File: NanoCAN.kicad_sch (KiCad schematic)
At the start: 18 parts, among them J2 Screw_Terminal_01x02, J3 Screw_Terminal_01x02, SW1 SW_DIP_x01, U1 MCP2557FD-xSN, U3 MCP2517FD-xJHA, Y1 Crystal_GND24

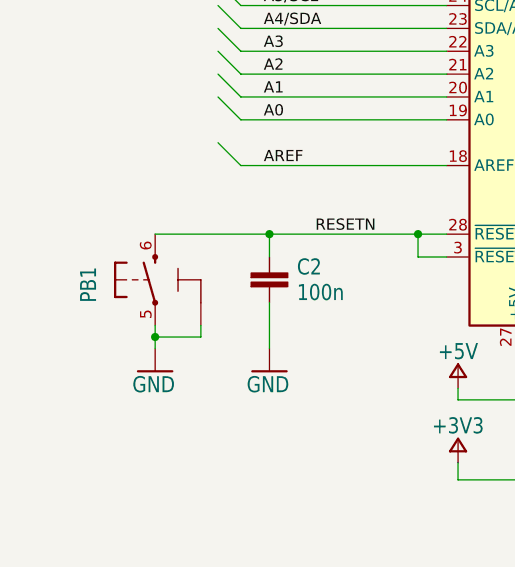
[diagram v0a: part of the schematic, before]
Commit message: Swap pushbutton for PTS810 and create 3D Model
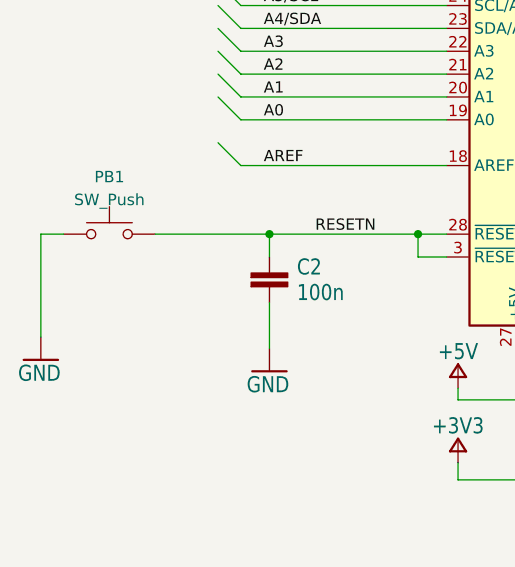
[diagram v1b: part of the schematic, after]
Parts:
- removed PB1: TACTILE1PTS820-NH, NANOEveryV3.0:C&K_PTS820_NO_HOLES, symbol NANOEveryV3.0-eagle-import:TACTILE1PTS820-NH
- added PB1: SW_Push, Button_Switch_SMD:SW_SPST_PTS810, symbol Switch:SW_Push
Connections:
- net GND: now also PB1.1
- net RESETN: now also PB1.2
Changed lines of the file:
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@@
   (junction (at 349.885 150.495) (diameter 0) (color 0 0 0 0)
   )
-  (junction (at 167.64 195.58) (diameter 0) (color 0 0 0 0)
-  )
   (junction (at 259.08 172.72) (diameter 0) (color 0 0 0 0)
   )
@@
     (stroke (width 0) (type default))
   )
-  (wire (pts (xy 172.72 195.58) (xy 172.72 194.31))
+  (wire (pts (xy 154.94 184.15) (xy 154.94 195.58))
     (stroke (width 0.1524) (type solid))
   )
@@
     (stroke (width 0) (type default))
   )
-  (wire (pts (xy 167.64 195.58) (xy 172.72 195.58))
-    (stroke (width 0.1524) (type solid))
-  )
   (wire (pts (xy 200.025 176.53) (xy 177.165 176.53))
     (stroke (width 0.1524) (type solid))
@@
     (stroke (width 0.1524) (type solid))
   )
-  (wire (pts (xy 167.64 194.31) (xy 167.64 195.58))
-    (stroke (width 0.1524) (type solid))
-  )
   (wire (pts (xy 309.88 161.29) (xy 333.375 161.29))
     (stroke (width 0) (type default))
@@
     (stroke (width 0) (type default))
   )
-  (wire (pts (xy 167.64 195.58) (xy 167.64 196.85))
-    (stroke (width 0.1524) (type solid))
-  )
   (wire (pts (xy 375.92 184.785) (xy 375.92 183.515))
     (stroke (width 0) (type default))
@@
   )
   (wire (pts (xy 225.425 173.99) (xy 245.745 173.99))
+    (stroke (width 0.1524) (type solid))
+  )
+  (wire (pts (xy 154.94 184.15) (xy 157.48 184.15))
     (stroke (width 0.1524) (type solid))
   )
@@
         (path "/a24b9486-fc79-44d2-a048-c84f452a13e3"
           (reference "#GND04") (unit 1)
+        )
+      )
+    )
+  )
+  (symbol (lib_id "Switch:SW_Push") (at 162.56 184.15 0) (unit 1)
+    (in_bom yes) (on_board yes) (dnp no) (fields_autoplaced)
+    (property "Reference" "PB1" (at 162.56 177.8 0)
+      (effects (font (size 1.27 1.27)))
+    )
+    (property "Value" "SW_Push" (at 162.56 180.34 0)
+      (effects (font (size 1.27 1.27)))
+    )
+    (property "Footprint" "Button_Switch_SMD:SW_SPST_PTS810" (at 162.56 179.07 0)
+      (effects (font (size 1.27 1.27)) hide)
+    )
+    (property "Datasheet" "~" (at 162.56 179.07 0)
+      (effects (font (size 1.27 1.27)) hide)
+    )
+    (pin "1")
+    (pin "2")
+    (instances
+      (project "NanoCAN"
+        (path "/a24b9486-fc79-44d2-a048-c84f452a13e3"
+          (reference "PB1") (unit 1)
         )
       )
@@
     )
   )
-  (symbol (lib_id "NANOEveryV3.0-eagle-import:TACTILE1PTS820-NH") (at 167.64 189.23 0) (unit 1)
-    (in_bom yes) (on_board yes) (dnp no)
-    (property "Reference" "PB1" (at 161.29 191.77 90)
-      (effects (font (size 1.778 1.5113)) (justify left bottom))
-    )
-    (property "Value" "TACTILE1PTS820-NH" (at 167.64 189.23 0)
-      (effects (font (size 1.27 1.27)) hide)
-    )
-    (property "Footprint" "NANOEveryV3.0:C&K_PTS820_NO_HOLES" (at 167.64 189.23 0)
-      (effects (font (size 1.27 1.27)) hide)
-    )
-    (property "Datasheet" "" (at 167.64 189.23 0)
-      (effects (font (size 1.27 1.27)) hide)
-    )
-    (pin "1")
-    (pin "2")
-    (pin "3")
-    (pin "4")
-    (pin "5")
-    (pin "6")
-    (instances
-      (project "NanoCAN"
-        (path "/a24b9486-fc79-44d2-a048-c84f452a13e3"
-          (reference "PB1") (unit 1)
-        )
-      )
-    )
-  )
   (symbol (lib_id "Device:R") (at 375.92 179.705 180) (unit 1)
     (in_bom yes) (on_board yes) (dnp no)
@@
     )
   )
-  (symbol (lib_id "NANOEveryV3.0-eagle-import:Arduino-supply_GND") (at 167.64 199.39 0) (unit 1)
-    (in_bom yes) (on_board yes) (dnp no)
-    (property "Reference" "#GND017" (at 167.64 199.39 0)
-      (effects (font (size 1.27 1.27)) hide)
-    )
-    (property "Value" "GND" (at 165.1 201.93 0)
+  (symbol (lib_id "NANOEveryV3.0-eagle-import:Arduino-supply_GND") (at 154.94 198.12 0) (unit 1)
+    (in_bom yes) (on_board yes) (dnp no)
+    (property "Reference" "#GND017" (at 154.94 198.12 0)
+      (effects (font (size 1.27 1.27)) hide)
+    )
+    (property "Value" "GND" (at 152.4 200.66 0)
       (effects (font (size 1.778 1.5113)) (justify left bottom))
     )
-    (property "Footprint" "" (at 167.64 199.39 0)
-      (effects (font (size 1.27 1.27)) hide)
-    )
-    (property "Datasheet" "" (at 167.64 199.39 0)
-      (effects (font (size 1.27 1.27)) hide)
-    )
+    (property "Footprint" "" (at 154.94 198.12 0)
+      (effects (font (size 1.27 1.27)) hide)
+    )
+    (property "Datasheet" "" (at 154.94 198.12 0)
+      (effects (font (size 1.27 1.27)) hide)
+    )

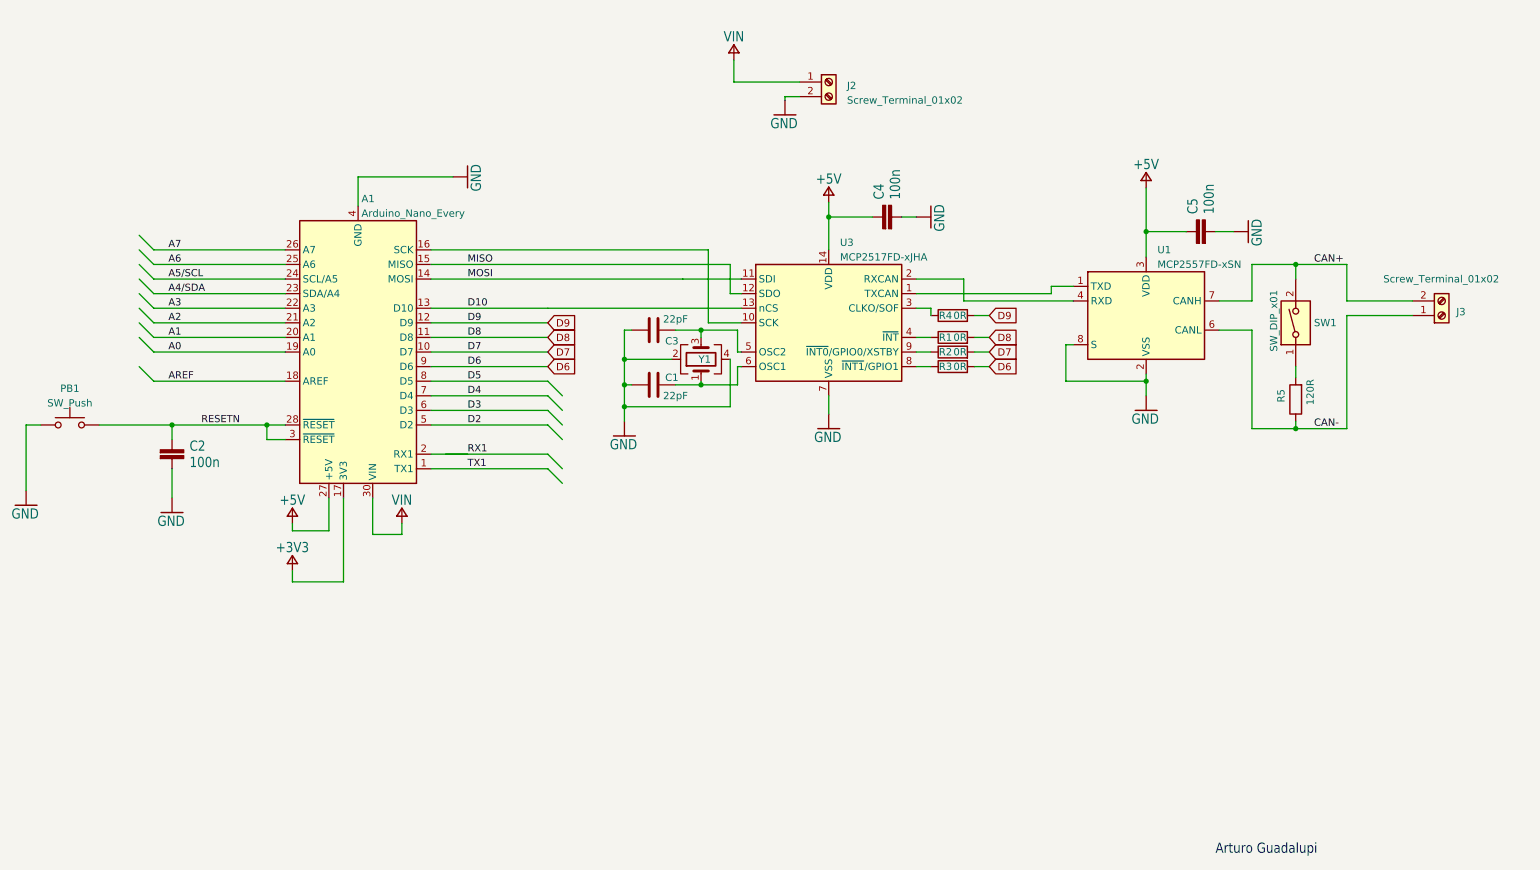
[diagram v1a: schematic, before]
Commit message: Update to MCP251863 to combine transciever and SPI converter
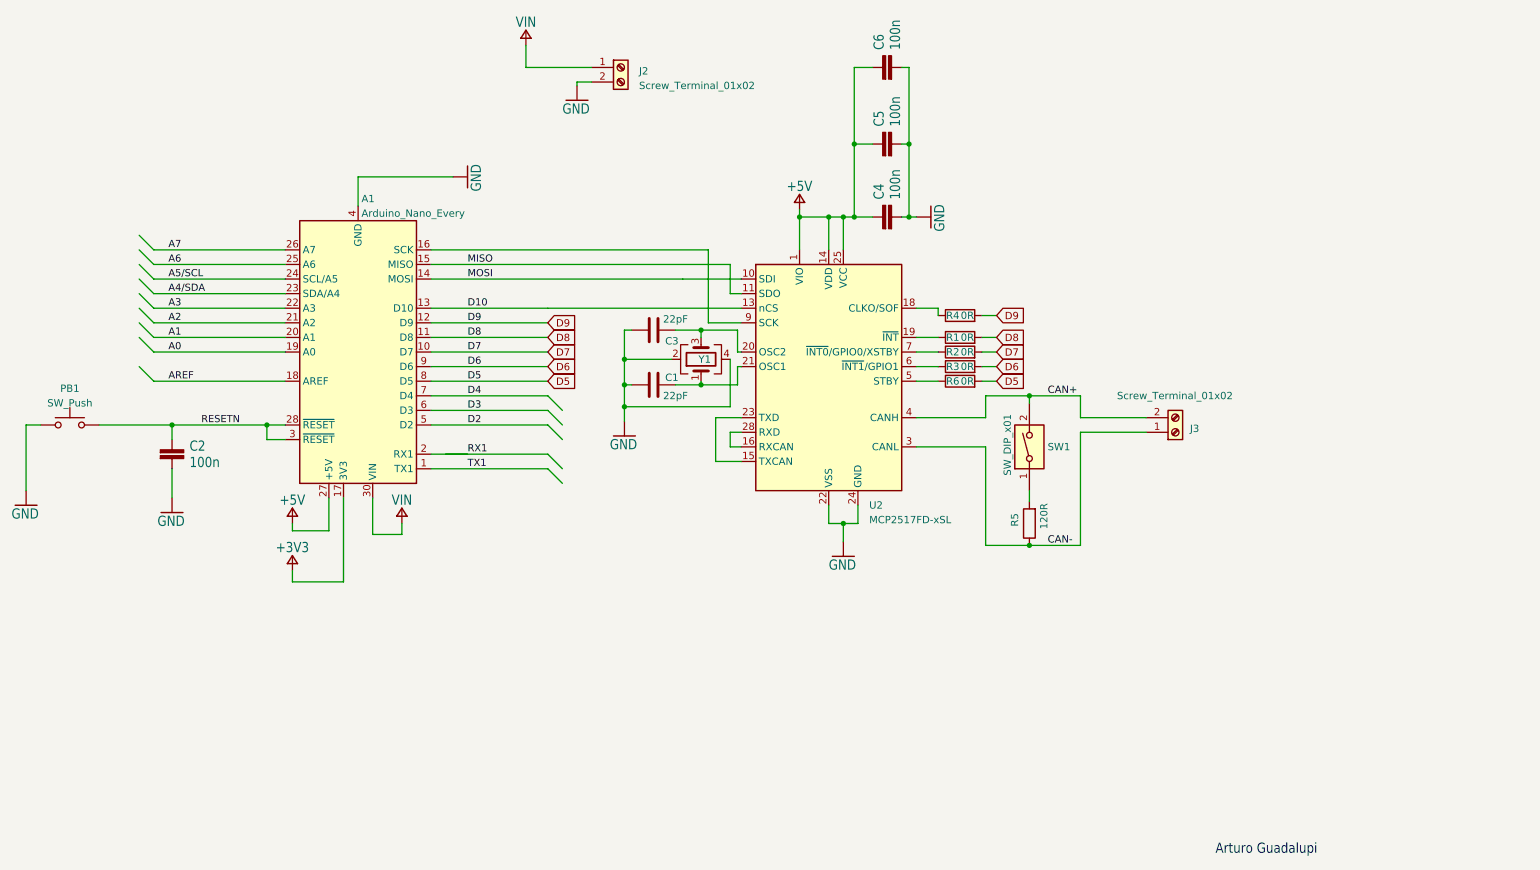
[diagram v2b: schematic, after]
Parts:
- removed U1: MCP2557FD-xSN, Package_SO:SOIC-8_3.9x4.9mm_P1.27mm, symbol Interface_CAN_LIN:MCP2557FD-xSN
- removed U3: MCP2517FD-xJHA, Package_DFN_QFN:DFN-14-1EP_3x4.5mm_P0.65mm_EP1.65x4.25mm, symbol Interface_CAN_LIN:MCP2517FD-xJHA
- added C6: 100n, Capacitor_SMD:C_0402_1005Metric_Pad0.74x0.62mm_HandSolder, symbol NANOEveryV3.0-eagle-import:C-0402
- added R6: 0R, Resistor_SMD:R_01005_0402Metric_Pad0.57x0.30mm_HandSolder, symbol Device:R
- added U2: MCP2517FD-xSL, Package_SO:SSOP-28_5.3x10.2mm_P0.65mm, symbol NanoCAN:MCP251863
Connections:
- net +5V: now also C6.1, U2.1 (VIO), U2.14 (VDD), U2.25 (VCC)
- net CAN+: now also U2.4 (CANH)
- net CAN-: now also U2.3 (CANL)
- net D10~{}: now also U2.13 (nCS)
- net D5~{}: now also R6.2
- net GND: now also C6.2, U2.22 (VSS), U2.24 (GND)
- net MISO: now also U2.11 (SDO)
- net MOSI: now also U2.10 (SDI)
- net at C3.2, Y1.3: now also U2.20 (OSC2)
- net at R1.1: now also U2.19 (~{INT})
- net at A1.16 (SCK): now also U2.9 (SCK)
- net at R2.1: now also U2.7 (~{INT0}/GPIO0/XSTBY)
- net at R4.1: now also U2.18 (CLKO/SOF)
- net at C1.2, Y1.1: now also U2.21 (OSC1)
- net at R3.1: now also U2.6 (~{INT1}/GPIO1)
- new net: U2.15 (TXCAN), U2.23 (TXD)
- new net: U2.16 (RXCAN), U2.28 (RXD)
- new net: R6.1, U2.5 (STBY)
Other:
- moved on the sheet: C5, J2, J3, R1, R2, R3, R4, R5, SW1
